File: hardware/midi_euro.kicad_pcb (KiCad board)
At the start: 2 copper layers, 104.1 x 55.9 mm, 11 parts, among them J1 Conn_02x05_Top_Bottom, J2 CUI_SD-50BV, J3 Thonkiconn, J4 Conn_ARM_JTAG_SWD_10, U1 LM1117-3.3, U2 SOT23_5V LDO, U3 STM32F030C8Tx

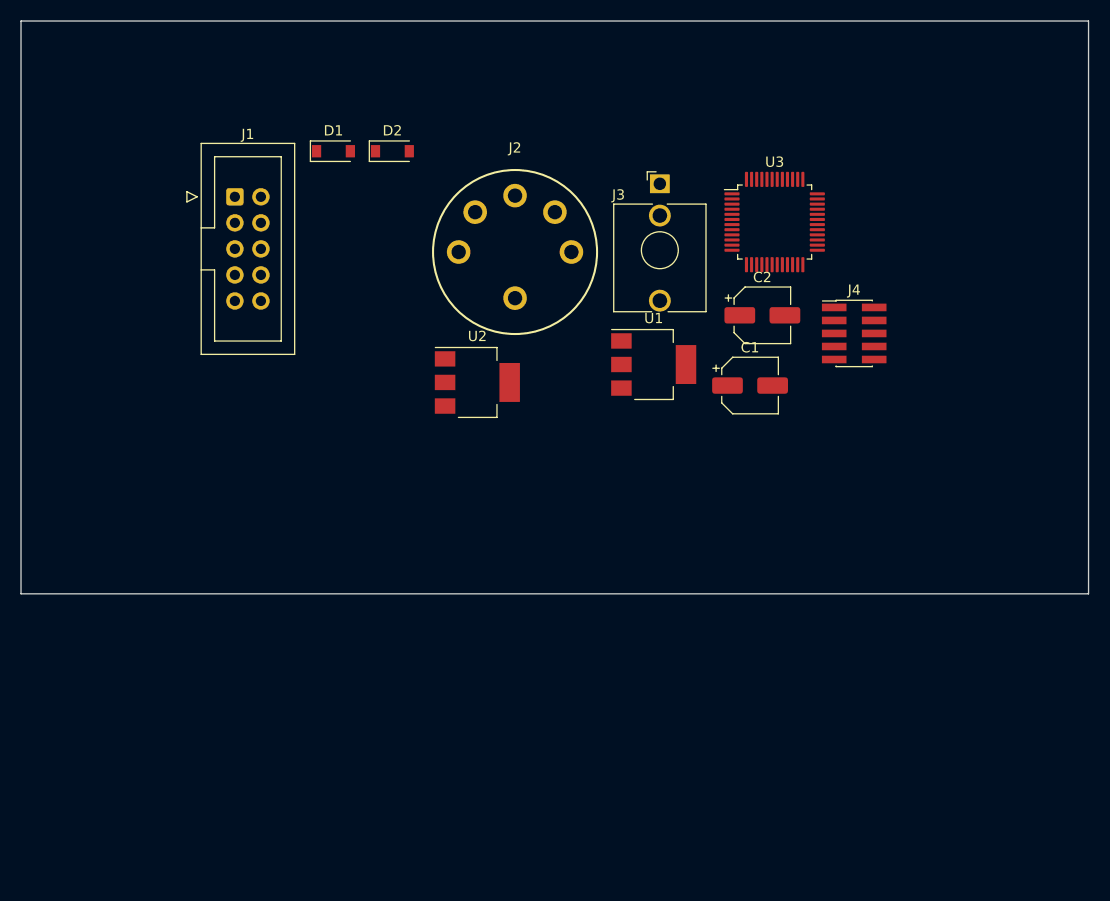
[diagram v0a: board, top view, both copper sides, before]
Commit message: MAX5715BAUD lib added
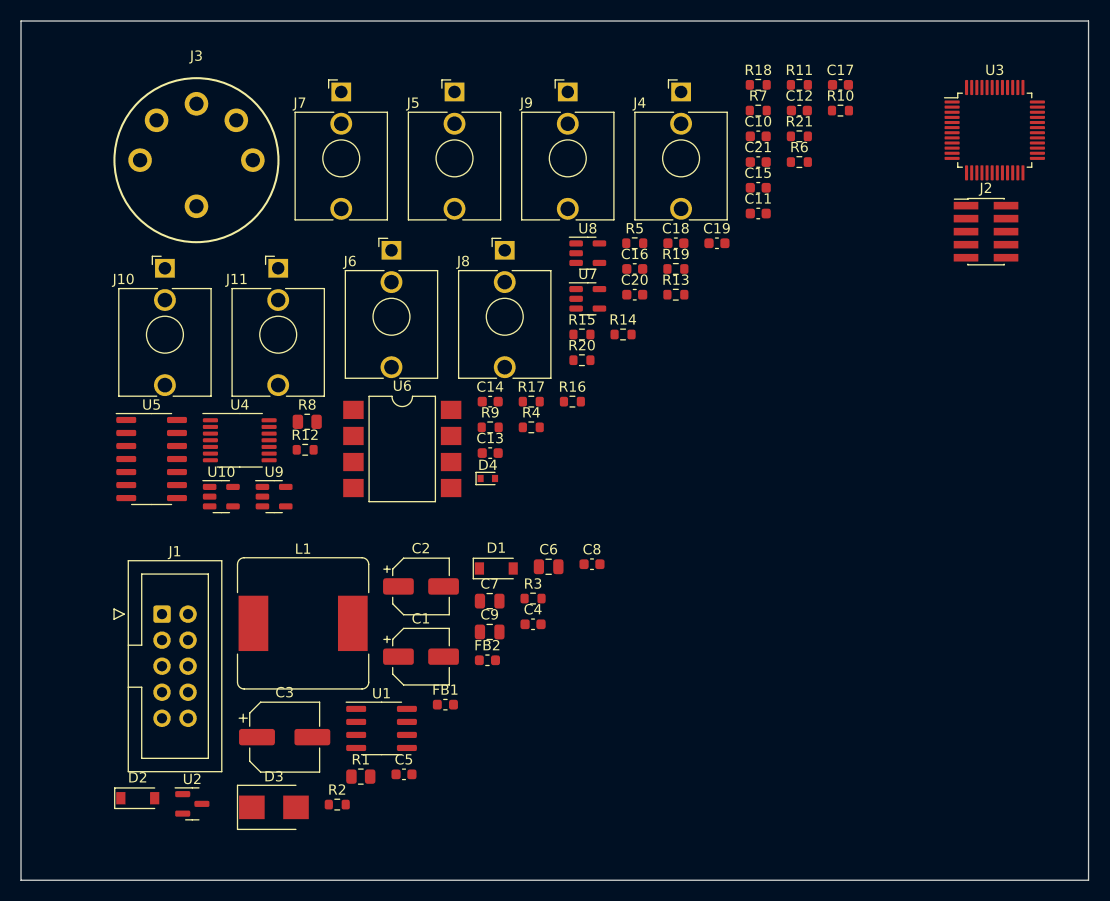
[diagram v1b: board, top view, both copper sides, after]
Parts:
- added C10: 100nF, Capacitor_SMD:C_0603_1608Metric, F.Cu at (127.8, 62.0)
- added C11: 100nF, Capacitor_SMD:C_0603_1608Metric, F.Cu at (127.8, 69.6)
- added C12: 100nF, Capacitor_SMD:C_0603_1608Metric, F.Cu at (131.8, 59.5)
- added C13: 100nF, Capacitor_SMD:C_0603_1608Metric, F.Cu at (101.7, 93.0)
- added C14: 18p, Capacitor_SMD:C_0603_1608Metric, F.Cu at (101.7, 87.9)
- added C15: 18p, Capacitor_SMD:C_0603_1608Metric, F.Cu at (127.8, 67.1)
- added C16: 18p, Capacitor_SMD:C_0603_1608Metric, F.Cu at (115.8, 75.0)
- added C17: 18p, Capacitor_SMD:C_0603_1608Metric, F.Cu at (135.8, 57.0)
- added C18: 100nF, Capacitor_SMD:C_0603_1608Metric, F.Cu at (119.8, 72.5)
- added C19: 100nF, Capacitor_SMD:C_0603_1608Metric, F.Cu at (123.8, 72.5)
- added C20: 100nF, Capacitor_SMD:C_0603_1608Metric, F.Cu at (115.8, 77.5)
- added C21: 100nF, Capacitor_SMD:C_0603_1608Metric, F.Cu at (127.8, 64.6)
- added C3: 100uF, Capacitor_SMD:CP_Elec_6.3x7.7, F.Cu at (81.6, 120.7)
- added C4: 100nF, Capacitor_SMD:C_0603_1608Metric, F.Cu at (105.8, 109.7)
- added C5: 100nF, Capacitor_SMD:C_0603_1608Metric, F.Cu at (93.2, 124.3)
- added C6: 22uF, Capacitor_SMD:C_0805_2012Metric, F.Cu at (107.3, 104.0)
- added C7: 22uF, Capacitor_SMD:C_0805_2012Metric, F.Cu at (101.6, 107.4)
- added C8: 100nF, Capacitor_SMD:C_0603_1608Metric, F.Cu at (111.6, 103.8)
- added C9: 22uF, Capacitor_SMD:C_0805_2012Metric, F.Cu at (101.6, 110.4)
- added D3: B220, Diode_SMD:D_SMB, F.Cu at (80.5, 127.5)
- added D4: 1N4148WT, Diode_SMD:D_SOD-523, F.Cu at (101.4, 95.4)
- added FB1: FerriteBead, Inductor_SMD:L_0603_1608Metric, F.Cu at (97.3, 117.5)
- added FB2: FerriteBead, Inductor_SMD:L_0603_1608Metric, F.Cu at (101.4, 113.2)
- added J10: Thonkiconn, Connector_Audio:Jack_3.5mm_QingPu_WQP-PJ398SM_Vertical_CircularHoles, F.Cu at (69.9, 74.9)
- added J11: Thonkiconn, Connector_Audio:Jack_3.5mm_QingPu_WQP-PJ398SM_Vertical_CircularHoles, F.Cu at (81.0, 74.9)
- added J5: Thonkiconn, Connector_Audio:Jack_3.5mm_QingPu_WQP-PJ398SM_Vertical_CircularHoles, F.Cu at (98.2, 57.7)
- added J6: Thonkiconn, Connector_Audio:Jack_3.5mm_QingPu_WQP-PJ398SM_Vertical_CircularHoles, F.Cu at (92.0, 73.2)
- added J7: Thonkiconn, Connector_Audio:Jack_3.5mm_QingPu_WQP-PJ398SM_Vertical_CircularHoles, F.Cu at (87.1, 57.7)
- added J8: Thonkiconn, Connector_Audio:Jack_3.5mm_QingPu_WQP-PJ398SM_Vertical_CircularHoles, F.Cu at (103.1, 73.2)
- added J9: Thonkiconn, Connector_Audio:Jack_3.5mm_QingPu_WQP-PJ398SM_Vertical_CircularHoles, F.Cu at (109.2, 57.7)
- added L1: SRR1260-221K, Inductor_SMD:L_Bourns_SRR1260, F.Cu at (83.4, 109.6)
- added R1: 0, Resistor_SMD:R_0805_2012Metric, F.Cu at (89.0, 124.5)
- added R10: 47k, Resistor_SMD:R_0603_1608Metric, F.Cu at (135.8, 59.5)
- added R11: 47k, Resistor_SMD:R_0603_1608Metric, F.Cu at (131.8, 57.0)
- added R12: 47k, Resistor_SMD:R_0603_1608Metric, F.Cu at (83.6, 92.6)
- added R13: 47k, Resistor_SMD:R_0603_1608Metric, F.Cu at (119.8, 77.5)
- added R14: 240k, Resistor_SMD:R_0603_1608Metric, F.Cu at (114.6, 81.4)
- added R15: 240k, Resistor_SMD:R_0603_1608Metric, F.Cu at (110.6, 81.4)
- added R16: 240k, Resistor_SMD:R_0603_1608Metric, F.Cu at (109.7, 87.9)
- added R17: 240k, Resistor_SMD:R_0603_1608Metric, F.Cu at (105.7, 87.9)
- added R18: 1k, Resistor_SMD:R_0603_1608Metric, F.Cu at (127.8, 57.0)
- added R19: 1k, Resistor_SMD:R_0603_1608Metric, F.Cu at (119.8, 75.0)
- added R2: 1Meg, Resistor_SMD:R_0603_1608Metric, F.Cu at (86.7, 127.2)
- added R20: 1k, Resistor_SMD:R_0603_1608Metric, F.Cu at (110.6, 83.9)
- added R21: 1k, Resistor_SMD:R_0603_1608Metric, F.Cu at (131.8, 62.0)
- added R3: 274k, Resistor_SMD:R_0603_1608Metric, F.Cu at (105.8, 107.1)
- added R4: 5k, Resistor_SMD:R_0603_1608Metric, F.Cu at (105.7, 90.4)
- added R5: 5k, Resistor_SMD:R_0603_1608Metric, F.Cu at (115.8, 72.5)
- added R6: 47k, Resistor_SMD:R_0603_1608Metric, F.Cu at (131.8, 64.6)
- added R7: 47k, Resistor_SMD:R_0603_1608Metric, F.Cu at (127.8, 59.5)
- added R8: 220, Resistor_SMD:R_0805_2012Metric, F.Cu at (83.8, 89.9)
- added R9: 10k, Resistor_SMD:R_0603_1608Metric, F.Cu at (101.7, 90.4)
- added U10: 74AHC1G125, Package_TO_SOT_SMD:SOT-23-5, F.Cu at (75.4, 97.2)
- added U4: MAX5815, Package_SO:TSSOP-14_4.4x5mm_P0.65mm, F.Cu at (77.2, 91.7)
- added U5: TL074, Package_SO:SOIC-14_3.9x8.7mm_P1.27mm, F.Cu at (68.6, 93.5)
- added U6: 6N138, Package_DIP:SMDIP-8_W9.53mm, F.Cu at (93.1, 92.5)
- added U7: 74AHC1G125, Package_TO_SOT_SMD:SOT-23-5, F.Cu at (111.2, 77.9)
- added U8: 74AHC1G125, Package_TO_SOT_SMD:SOT-23-5, F.Cu at (111.2, 73.5)
- added U9: 74AHC1G125, Package_TO_SOT_SMD:SOT-23-5, F.Cu at (80.6, 97.2)
- J2: value CUI_SD-50BV -> Conn_ARM_JTAG_SWD_10; footprint midi_euro_lib:CUI_SD-50BV -> Connector_PinHeader_1.27mm:PinHeader_2x05_P1.27mm_Vertical_SMD
- J3: value Thonkiconn -> CUI_SD-50BV; footprint Connector_Audio:Jack_3.5mm_QingPu_WQP-PJ398SM_Vertical_CircularHoles -> midi_euro_lib:CUI_SD-50BV
- J4: value Conn_ARM_JTAG_SWD_10 -> Thonkiconn; footprint Connector_PinHeader_1.27mm:PinHeader_2x05_P1.27mm_Vertical_SMD -> Connector_Audio:Jack_3.5mm_QingPu_WQP-PJ398SM_Vertical_CircularHoles
- U1: value LM1117-3.3 -> MAX5033B(A/U)SA; footprint Package_TO_SOT_SMD:SOT-223-3_TabPin2 -> Package_SO:SOIC-8_3.9x4.9mm_P1.27mm
- U2: value SOT23_5V LDO -> LM3480-3.3; footprint Package_TO_SOT_SMD:SOT-223-3_TabPin2 -> Package_TO_SOT_SMD:SOT-23
- moved D2 67.8 mm to (67.3, 126.6)
- moved U2 49.6 mm to (72.6, 127.2)
- moved J2 46.0 mm to (150.0, 71.3)
- moved J3 45.3 mm to (73.0, 64.4)
- moved U1 44.3 mm to (91.0, 119.8)
- moved D1 43.7 mm to (102.2, 104.2)
- moved C2 42.5 mm to (94.9, 106.0)
- moved C1 41.6 mm to (94.9, 112.8)
- moved J1 41.3 mm to (69.6, 108.7)
- moved J4 29.0 mm to (120.3, 57.7)
- moved U3 23.3 mm to (150.9, 61.5)
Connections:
- C1 pad 1: VCC -> +5V
- D1 pad 1: VCC -> +5V
- J1 pad 1: Net-(D1-Pad2) -> Net-(FB1-Pad2)
- J1 pad 10: unconnected-(J1-Pad10) -> Net-(FB2-Pad2)
- J1 pad 2: unconnected-(J1-Pad2) -> GND
- J1 pad 3: unconnected-(J1-Pad3) -> GND
- J1 pad 4: unconnected-(J1-Pad4) -> GND
- J1 pad 5: Net-(D2-Pad1) -> Net-(FB2-Pad2)
- J1 pad 6: unconnected-(J1-Pad6) -> Net-(FB1-Pad2)
- J2 pad 3: unconnected-(J2-Pad3) -> Net-(J2-Pad3)
- J2 pad 5: unconnected-(J2-Pad5) -> Net-(J2-Pad3)
- U1 pad 1: unconnected-(U1-Pad1) -> Net-(C5-Pad1)
- U1 pad 2: unconnected-(U1-Pad2) -> Net-(C4-Pad2)
- U1 pad 3: unconnected-(U1-Pad3) -> GND
- U2 pad 1: unconnected-(U2-Pad1) -> +3V3
- U2 pad 2: unconnected-(U2-Pad2) -> +5V
- U2 pad 3: unconnected-(U2-Pad3) -> GND
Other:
- board size 104.1 x 55.9 mm -> 104.1 x 83.8 mm

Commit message: chore: resync local state
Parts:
- added C18: 100nF, Capacitor_SMD:C_0603_1608Metric, F.Cu at (180.3, 71.1)
- added C19: 100nF, Capacitor_SMD:C_0603_1608Metric, F.Cu at (184.3, 73.6)
- added C20: 100nF, Capacitor_SMD:C_0603_1608Metric, F.Cu at (181.1, 63.6)
- added C21: 100nF, Capacitor_SMD:C_0603_1608Metric, F.Cu at (184.3, 71.1)
- added C22: 100n, Capacitor_SMD:C_0603_1608Metric, F.Cu at (134.6, 106.7)
- added C23: 100n, Capacitor_SMD:C_0603_1608Metric, F.Cu at (143.1, 103.7)
- added C24: 100n, Capacitor_SMD:C_0603_1608Metric, F.Cu at (134.6, 109.2)
- added C25: 100n, Capacitor_SMD:C_0603_1608Metric, F.Cu at (142.6, 106.2)
- added C26: 4.7uF, Capacitor_SMD:C_0805_2012Metric, F.Cu at (134.8, 103.9)
- added C27: 100n, Capacitor_SMD:C_0603_1608Metric, F.Cu at (138.6, 106.7)
- added C28: 18p, Capacitor_SMD:C_0603_1608Metric, F.Cu at (185.1, 63.6)
- added C29: 18p, Capacitor_SMD:C_0603_1608Metric, F.Cu at (185.1, 68.6)
- added C30: 18p, Capacitor_SMD:C_0603_1608Metric, F.Cu at (185.1, 66.1)
- added C31: 18p, Capacitor_SMD:C_0603_1608Metric, F.Cu at (181.1, 68.6)
- added C32: 100nF, Capacitor_SMD:C_0603_1608Metric, F.Cu at (179.3, 96.0)
- added C33: 100nF, Capacitor_SMD:C_0603_1608Metric, F.Cu at (169.0, 103.0)
- added C34: 100nF, Capacitor_SMD:C_0603_1608Metric, F.Cu at (173.0, 100.5)
- added C35: 100nF, Capacitor_SMD:C_0603_1608Metric, F.Cu at (169.0, 100.5)
- added D4: 1N4148WT, Diode_SMD:D_SOD-523, F.Cu at (249.3, 48.1)
- added J10: Thonkiconn, Connector_Audio:Jack_3.5mm_QingPu_WQP-PJ398SM_Vertical_CircularHoles, F.Cu at (178.4, 48.8)
- added J11: Thonkiconn, Connector_Audio:Jack_3.5mm_QingPu_WQP-PJ398SM_Vertical_CircularHoles, F.Cu at (167.4, 48.8)
- added J12: Thonkiconn, Connector_Audio:Jack_3.5mm_QingPu_WQP-PJ398SM_Vertical_CircularHoles, F.Cu at (189.5, 81.2)
- added J13: Thonkiconn, Connector_Audio:Jack_3.5mm_QingPu_WQP-PJ398SM_Vertical_CircularHoles, F.Cu at (200.5, 81.2)
- added J14: Thonkiconn, Connector_Audio:Jack_3.5mm_QingPu_WQP-PJ398SM_Vertical_CircularHoles, F.Cu at (167.4, 81.2)
- added J15: Thonkiconn, Connector_Audio:Jack_3.5mm_QingPu_WQP-PJ398SM_Vertical_CircularHoles, F.Cu at (178.4, 81.2)
- added J3: CUI_SD-50BV, midi_euro_lib:CUI_SD-50BV, F.Cu at (225.7, 55.5)
- added J8: Thonkiconn, Connector_Audio:Jack_3.5mm_QingPu_WQP-PJ398SM_Vertical_CircularHoles, F.Cu at (189.5, 48.8)
- added J9: Thonkiconn, Connector_Audio:Jack_3.5mm_QingPu_WQP-PJ398SM_Vertical_CircularHoles, F.Cu at (200.5, 48.8)
- added R22: n.a., Resistor_SMD:R_0603_1608Metric, F.Cu at (138.6, 109.2)
- added R23: 0, Resistor_SMD:R_0603_1608Metric, F.Cu at (139.1, 103.7)
- added R24: 5k, Resistor_SMD:R_0603_1608Metric, F.Cu at (189.1, 68.6)
- added R25: 5k, Resistor_SMD:R_0603_1608Metric, F.Cu at (208.1, 48.1)
- added R26: 47k, Resistor_SMD:R_0603_1608Metric, F.Cu at (180.3, 73.6)
- added R27: 47k, Resistor_SMD:R_0603_1608Metric, F.Cu at (181.1, 66.1)
- added R28: 47k, Resistor_SMD:R_0603_1608Metric, F.Cu at (172.3, 70.1)
- added R29: 47k, Resistor_SMD:R_0603_1608Metric, F.Cu at (193.1, 63.6)
- added R30: 47k, Resistor_SMD:R_0603_1608Metric, F.Cu at (176.3, 70.1)
- added R31: 47k, Resistor_SMD:R_0603_1608Metric, F.Cu at (167.9, 73.8)
- added R32: 240k, Resistor_SMD:R_0603_1608Metric, F.Cu at (189.1, 66.1)
- added R33: 240k, Resistor_SMD:R_0603_1608Metric, F.Cu at (212.1, 48.1)
- added R34: 240k, Resistor_SMD:R_0603_1608Metric, F.Cu at (193.1, 66.1)
- added R35: 240k, Resistor_SMD:R_0603_1608Metric, F.Cu at (176.3, 72.7)
- added R36: 1k, Resistor_SMD:R_0603_1608Metric, F.Cu at (208.1, 50.6)
- added R37: 1k, Resistor_SMD:R_0603_1608Metric, F.Cu at (189.1, 63.6)
- added R38: 1k, Resistor_SMD:R_0603_1608Metric, F.Cu at (172.3, 72.7)
- added R39: 1k, Resistor_SMD:R_0603_1608Metric, F.Cu at (163.9, 73.8)
- added R8: 220, Resistor_SMD:R_0805_2012Metric, F.Cu at (236.6, 60.1)
- added R9: 10k, Resistor_SMD:R_0603_1608Metric, F.Cu at (219.2, 65.3)
- added U10: 74AHC1G125, Package_TO_SOT_SMD:SOT-23-5, F.Cu at (164.4, 101.4)
- added U11: 74AHC1G125, Package_TO_SOT_SMD:SOT-23-5, F.Cu at (169.6, 97.0)
- added U12: 74AHC1G125, Package_TO_SOT_SMD:SOT-23-5, F.Cu at (164.4, 97.0)
- added U6: 6N138, Package_DIP:SMDIP-8_W9.53mm, F.Cu at (240.9, 52.8)
- added U7: MAX5815, Package_SO:TSSOP-14_4.4x5mm_P0.65mm, F.Cu at (174.7, 65.6)
- added U8: TL074, Package_SO:SOIC-14_3.9x8.7mm_P1.27mm, F.Cu at (166.1, 67.4)
- added U9: 74AHC1G125, Package_TO_SOT_SMD:SOT-23-5, F.Cu at (174.7, 97.0)
- J1: moved to B.Cu
- moved J4 105.0 mm to (17.8, 80.6)
- moved L1 88.2 mm to (116.8, 27.9), turned to -90 degrees
- moved J1 85.0 mm to (36.3, 30.5), turned to 180 degrees
- moved J5 80.8 mm to (17.8, 65.3)
- moved U3 79.5 mm to (78.7, 27.9)
- moved J6 77.6 mm to (17.8, 95.8)
- moved J9 76.6 mm to (33.0, 65.3)
- moved J2 74.8 mm to (80.7, 43.2)
- moved J8 73.6 mm to (33.0, 95.8)
- moved U4 65.8 mm to (61.0, 27.9)
- moved U6 65.4 mm to (53.3, 40.6)
- moved J3 61.5 mm to (25.4, 25.4)
- moved J10 57.7 mm to (17.8, 50.1)
- moved J7 54.6 mm to (33.0, 50.1)
- moved J11 48.3 mm to (33.0, 80.6)
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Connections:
- net /IOs/dac_clr renamed /pitch/dac_clr
- net /IOs/dac_ref renamed /pitch/dac_ref
- net /IOs/dac_ref/2 renamed /pitch/dac_ref/2
- net /IOs/dac_scl renamed /pitch/I2C1_SCL
- net /IOs/dac_sda renamed /pitch/I2C1_SDA
- J2 pad 1: unconnected-(J2-Pad1) -> +3V3
- J2 pad 10: unconnected-(J2-Pad10) -> /controller/NRST
- J2 pad 2: unconnected-(J2-Pad2) -> /controller/SWDIO
- J2 pad 3: Net-(J2-Pad3) -> GND
- J2 pad 4: unconnected-(J2-Pad4) -> /controller/SWCLK
- J2 pad 5: Net-(J2-Pad3) -> GND
- J2 pad 9: unconnected-(J2-Pad9) -> GND
- U3 pad 1: unconnected-(U3-Pad1) -> +3V3
- U3 pad 23: unconnected-(U3-Pad23) -> GND
- U3 pad 34: unconnected-(U3-Pad34) -> /controller/SWDIO
- U3 pad 37: unconnected-(U3-Pad37) -> /controller/SWCLK
- U3 pad 42: unconnected-(U3-Pad42) -> /controller/I2C1_SCL
- U3 pad 43: unconnected-(U3-Pad43) -> /controller/I2C1_SDA
- U3 pad 44: unconnected-(U3-Pad44) -> Net-(R22-Pad2)
- U3 pad 47: unconnected-(U3-Pad47) -> GND
- U3 pad 7: unconnected-(U3-Pad7) -> /controller/NRST
- U3 pad 8: unconnected-(U3-Pad8) -> GND
- U3 pad 9: unconnected-(U3-Pad9) -> +3V3
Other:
- board size 104.1 x 83.8 mm -> 30 x 100 mm
